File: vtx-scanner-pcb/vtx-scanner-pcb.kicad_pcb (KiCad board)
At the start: 4 copper layers, 65.8 x 77.2 mm, 36 parts, among them CON1 SJ-3523-SMT-TR, J1 Conn_01x06_Male, J2 Conn_01x08_Female, J3 SMA-J-P-H-RA-TH1, J4 Conn_01x05, J5 XT60-M, Q1 MMSS8050-H-TP, Q2 MMSS8050-H-TP, Q3 MMSS8050-H-TP, U1 RX5808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

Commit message: Reworked PCB
 - missing pullups IO0/EN
 - added capacitors for EN
 - clearance around mounting holes
 - better 2.4GHz antenna placement
 - correct rx5808 size
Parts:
- removed the REF** at (72.4, 63.3)
- removed the REF** at (101.3, 63.4)
- removed the REF** at (72.4, 33.9)
- removed the REF** at (101.3, 33.9)
- added C4: 300nF, Capacitor_SMD:C_0805_2012Metric_Pad1.15x1.40mm_HandSolder, F.Cu at (67.3, 27.4)
- added R8: 10K, Resistor_SMD:R_1206_3216Metric_Pad1.42x1.75mm_HandSolder, F.Cu at (67.3, 30.5)
- added R9: 10K, Resistor_SMD:R_1206_3216Metric_Pad1.42x1.75mm_HandSolder, F.Cu at (100.9, 42.6)
- added REF**: MountingHole_3mm, MountingHole:MountingHole_3mm, F.Cu at (101.3, 35.0)
- added REF**: MountingHole_3mm, MountingHole:MountingHole_3mm, F.Cu at (71.1, 35.0)
- added REF**: MountingHole_3mm, MountingHole:MountingHole_3mm, F.Cu at (71.1, 63.4)
- added REF**: MountingHole_3mm, MountingHole:MountingHole_3mm, F.Cu at (101.4, 63.4)
- C3: value 10nF -> 100nF
- J2: value Conn_01x08_Female -> sh1106-1.3inch-oled; footprint Connector_PinHeader_2.54mm:PinHeader_1x08_P2.54mm_Horizontal -> deets:sh1106-1.3inch-oled; moved to F.Cu
- moved C3 10.6 mm to (72.6, 27.9), turned to 270 degrees
- moved J2 9.09 mm to (85.6, 63.0), turned to 0 degrees
- moved A1 6.61 mm to (84.7, 34.9)
- moved CON1 2.16 mm to (112.8, 43.8)
- moved S3 0.89 mm to (68.3, 77.5)
- moved S1 0.51 mm to (86.2, 83.8)
- moved S2 0.51 mm to (86.2, 70.5)
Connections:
- A1 pad 10: Net-(A1-Pad10) -> /SSD1306_DC
- A1 pad 23: /SSD1306_DC -> Net-(A1-Pad23)
- J2 pad 2: Net-(J2-Pad2) -> +3V3
- J2 pad 3: +3V3 -> /SSD1306_CLK
- J2 pad 4: /SSD1306_CS -> /SSD1306_DATA
- J2 pad 7: /SSD1306_CLK -> /SSD1306_CS
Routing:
- net /#EN: track 77.3 -> 94.2 mm
- net /IO0: track 45.9 -> 58.8 mm, vias 3 -> 5
- net Net-(A1-Pad34): track 66.0 -> 78.3 mm
- net /BUTTON_UP: track 47.9 -> 59.1 mm
- net /RX: track 83.7 -> 94.3 mm
- net /EXP1: track 22.1 -> 32.6 mm
- net /SSD1306_DC: track 21.4 -> 31.6 mm
- net /EXP2: track 43.9 -> 54.1 mm, vias 6 -> 1
- net -BATT: track 75.7 -> 85.3 mm, vias 29 -> 31
- net /BUTTON_LEFT: track 56.0 -> 64.2 mm
- net Net-(CON1-Pad2): track 21.6 -> 14.8 mm
- net +3V3: track 25.1 -> 31.7 mm, vias 9 -> 10
- net /VRX_DATA: track 30.9 -> 24.5 mm, vias 5 -> 2
- net /SSD1306_CLK: track 29.5 -> 34.6 mm, vias 0 -> 2
- net /SSD1306_CS: track 32.8 -> 37.5 mm, vias 2 -> 0
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
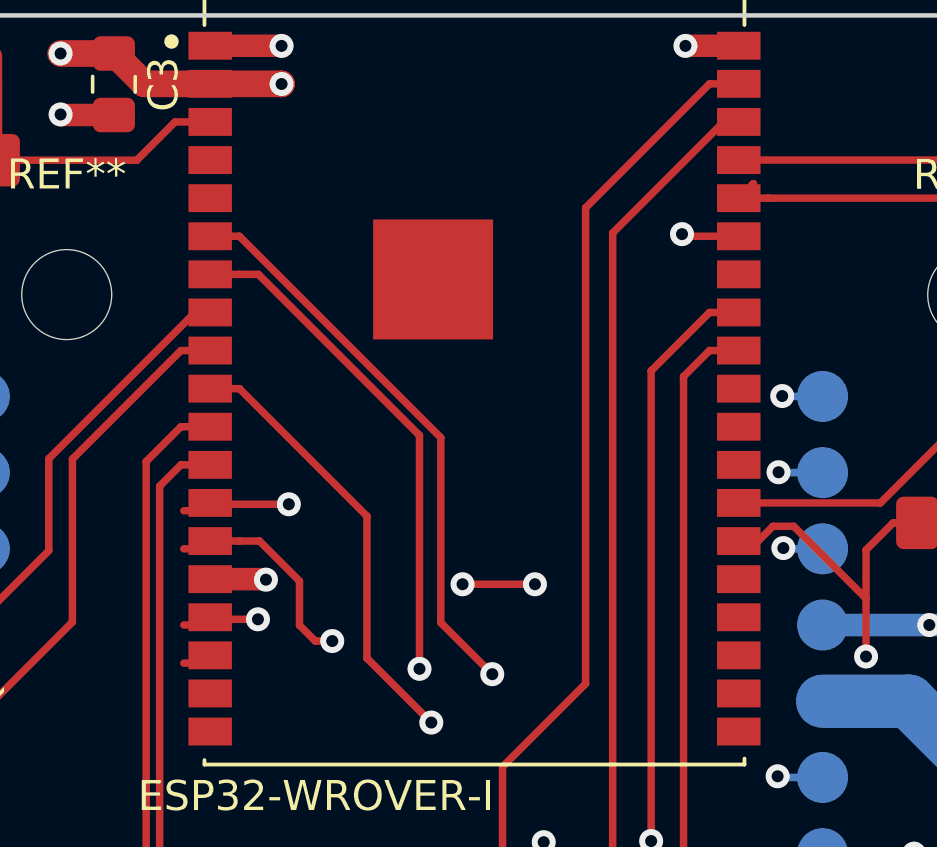
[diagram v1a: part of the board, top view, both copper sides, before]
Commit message: Removed a few superfluous track pieces
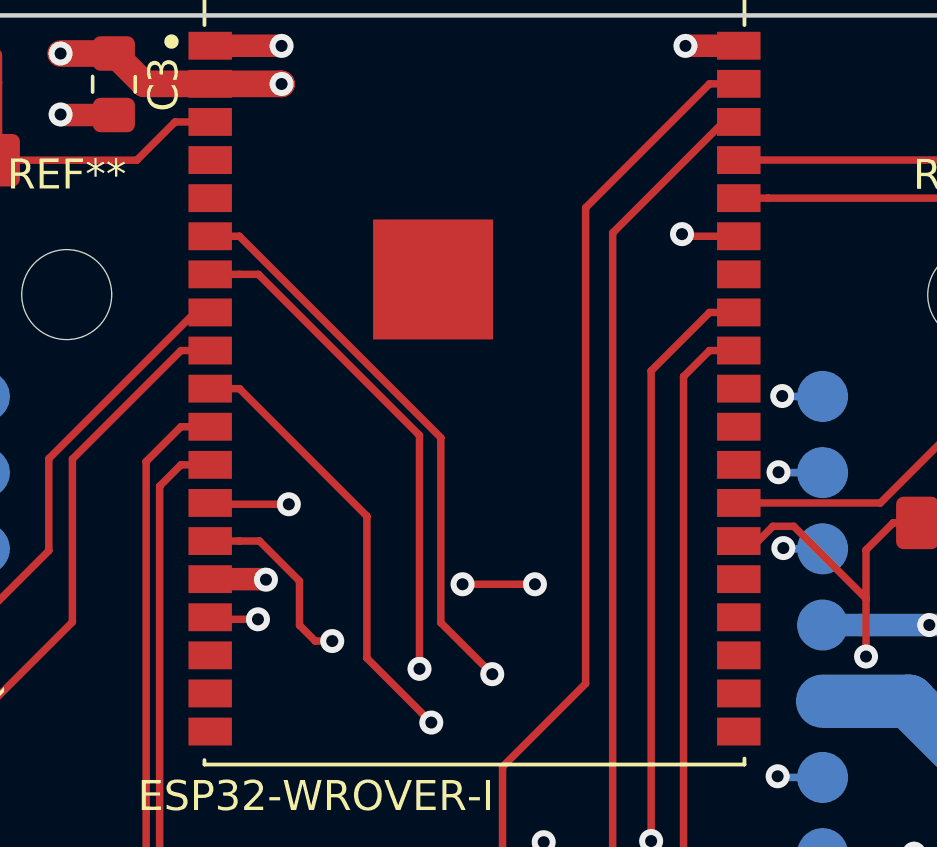
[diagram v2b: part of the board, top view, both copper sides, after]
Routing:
- net Net-(A1-Pad17): track 0.97 -> 0.00 mm
- net /VRX_CS: track 24.1 -> 23.1 mm
- net /VRX_CLOCK: track 24.9 -> 24.0 mm
- net /VRX_DATA: track 24.5 -> 23.5 mm
- net Net-(A1-Pad34): track 78.3 -> 77.6 mm
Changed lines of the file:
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@@
-(kicad_pcb (version 20171130) (host pcbnew "(5.1.0-0)")
+(kicad_pcb (version 20171130) (host pcbnew 5.0.2-bee76a0~70~ubuntu18.04.1)
   (general
     (thickness 1.6)
     (drawings 9)
-    (tracks 470)
+    (tracks 464)
     (zones 0)
     (modules 39)
@@
     (zone_45_only no)
     (trace_min 0.2)
+    (segment_width 0.2)
+    (edge_width 0.15)
     (via_size 0.8)
     (via_drill 0.4)
@@
     (uvia_min_size 0.2)
     (uvia_min_drill 0.1)
-    (edge_width 0.15)
-    (segment_width 0.2)
     (pcb_text_width 0.3)
     (pcb_text_size 1.5 1.5)
@@
   (segment (start 108.077 66.929) (end 107.95 66.802) (width 0.25) (layer In1.Cu) (net 6))
   (segment (start 107.95 66.802) (end 107.95 52.012998) (width 0.25) (layer F.Cu) (net 6))
-  (segment (start 93.951999 31.265001) (end 93.472 31.745) (width 0.25) (layer F.Cu) (net 6))
-  (segment (start 93.967001 31.265001) (end 93.951999 31.265001) (width 0.25) (layer F.Cu) (net 6))
   (segment (start 107.851001 36.925999) (end 102.670002 31.745) (width 0.25) (layer F.Cu) (net 6))
   (segment (start 94.447 31.745) (end 93.472 31.745) (width 0.25) (layer F.Cu) (net 6))
@@
   (segment (start 81.0768 42.3448) (end 76.827 38.095) (width 0.25) (layer F.Cu) (net 13))
   (segment (start 81.0768 47.0789) (end 81.0768 42.3448) (width 0.25) (layer F.Cu) (net 13))
-  (segment (start 74.971 47.244) (end 75.946 47.244) (width 0.25) (layer F.Cu) (net 19))
-  (segment (start 74.971 43.434) (end 75.946 43.434) (width 0.25) (layer F.Cu) (net 20))
   (via (at 94.9579 43.4086) (size 0.8) (drill 0.4) (layers F.Cu B.Cu) (net 20))
   (segment (start 94.9833 43.434) (end 94.9579 43.4086) (width 0.25) (layer B.Cu) (net 20))
@@
   (segment (start 78.8289 44.507298) (end 77.496602 43.175) (width 0.25) (layer F.Cu) (net 20))
   (segment (start 78.8289 45.981985) (end 78.8289 44.507298) (width 0.25) (layer F.Cu) (net 20))
-  (segment (start 74.971 45.974) (end 75.946 45.974) (width 0.25) (layer F.Cu) (net 21))
   (via (at 94.9198 38.3413) (size 0.8) (drill 0.4) (layers F.Cu B.Cu) (net 21))
   (segment (start 94.9325 38.354) (end 94.9198 38.3413) (width 0.25) (layer B.Cu) (net 21))
@@
   (segment (start 75.9205 45.7835) (end 75.852 45.715) (width 0.25) (layer F.Cu) (net 21))
   (segment (start 77.4446 45.7835) (end 75.9205 45.7835) (width 0.25) (layer F.Cu) (net 21))
-  (segment (start 74.971 42.164) (end 75.946 42.164) (width 0.25) (layer F.Cu) (net 22))
   (via (at 94.797002 40.8813) (size 0.8) (drill 0.4) (layers F.Cu B.Cu) (net 22))
   (segment (start 94.809702 40.894) (end 94.797002 40.8813) (width 0.25) (layer B.Cu) (net 22))
